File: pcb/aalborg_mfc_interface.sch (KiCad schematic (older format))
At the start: 19 parts, among them J1 DB15FV, J2 DB15FV, P1 PWR_JACK_2.5x5.5, P2 HEADER_01X03, U1 MAX6817

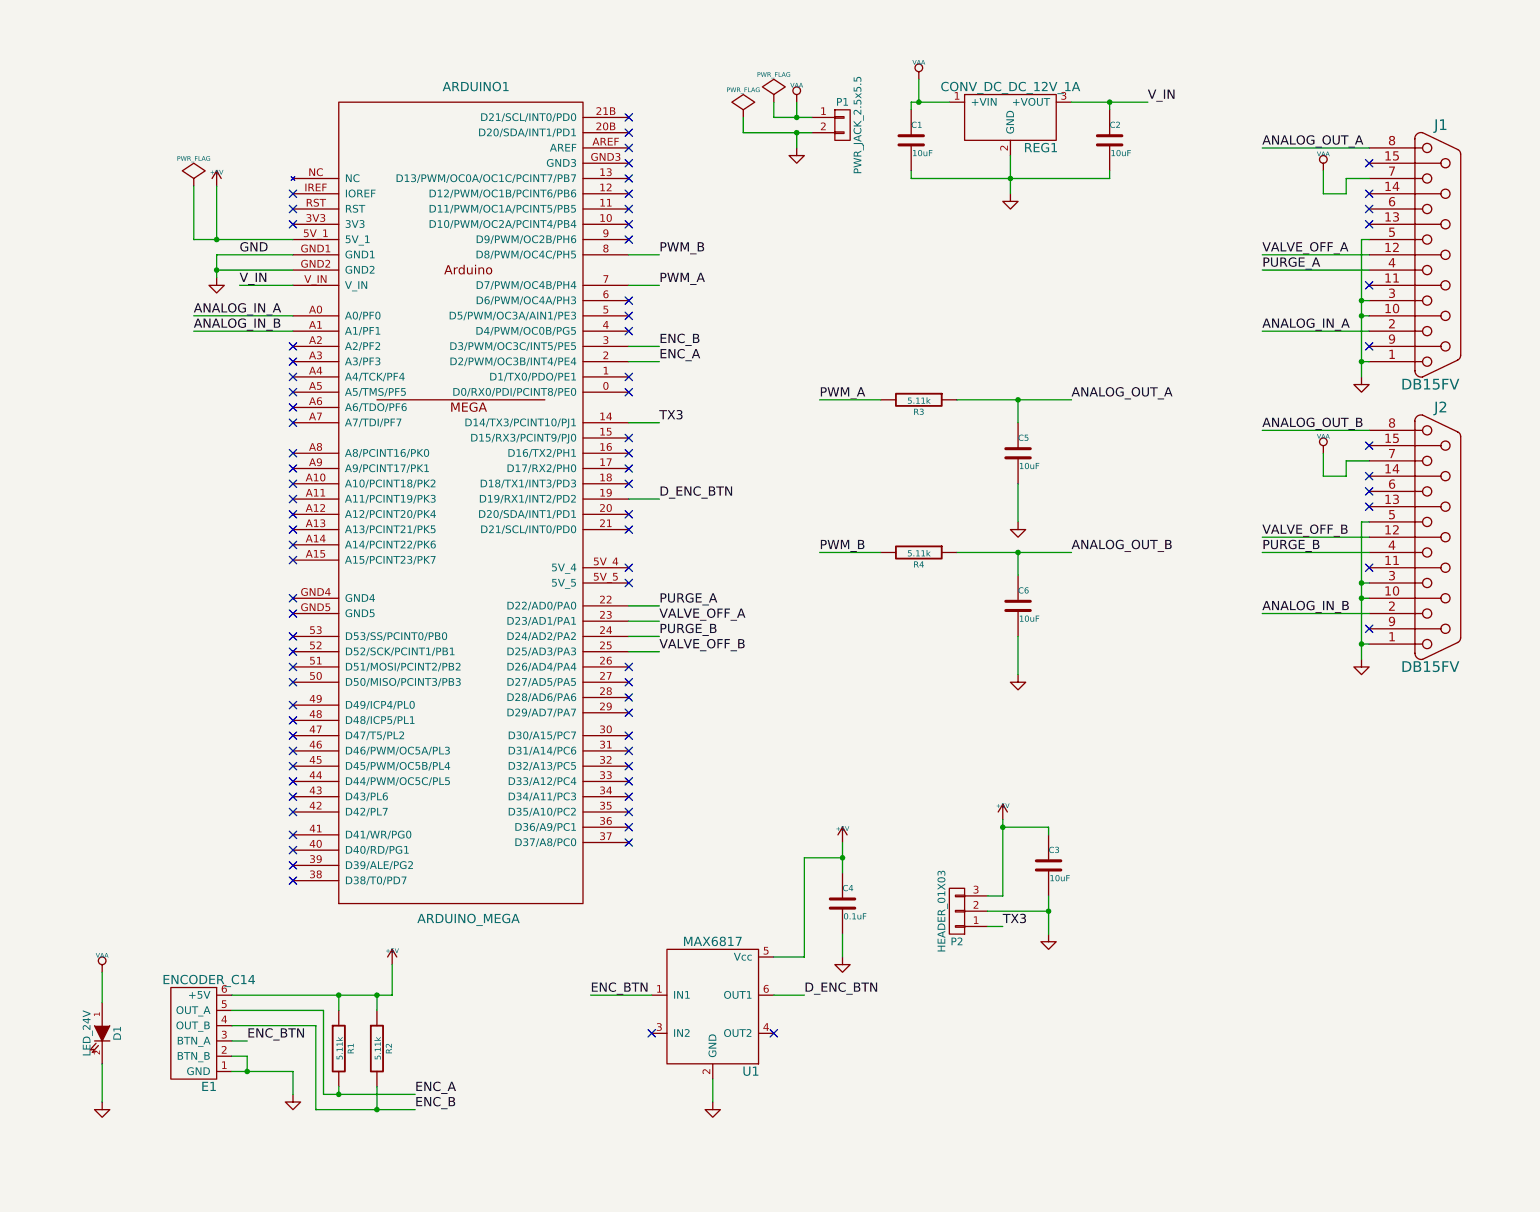
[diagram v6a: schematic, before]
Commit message: Updated design with changes first made to power_switch_controller.
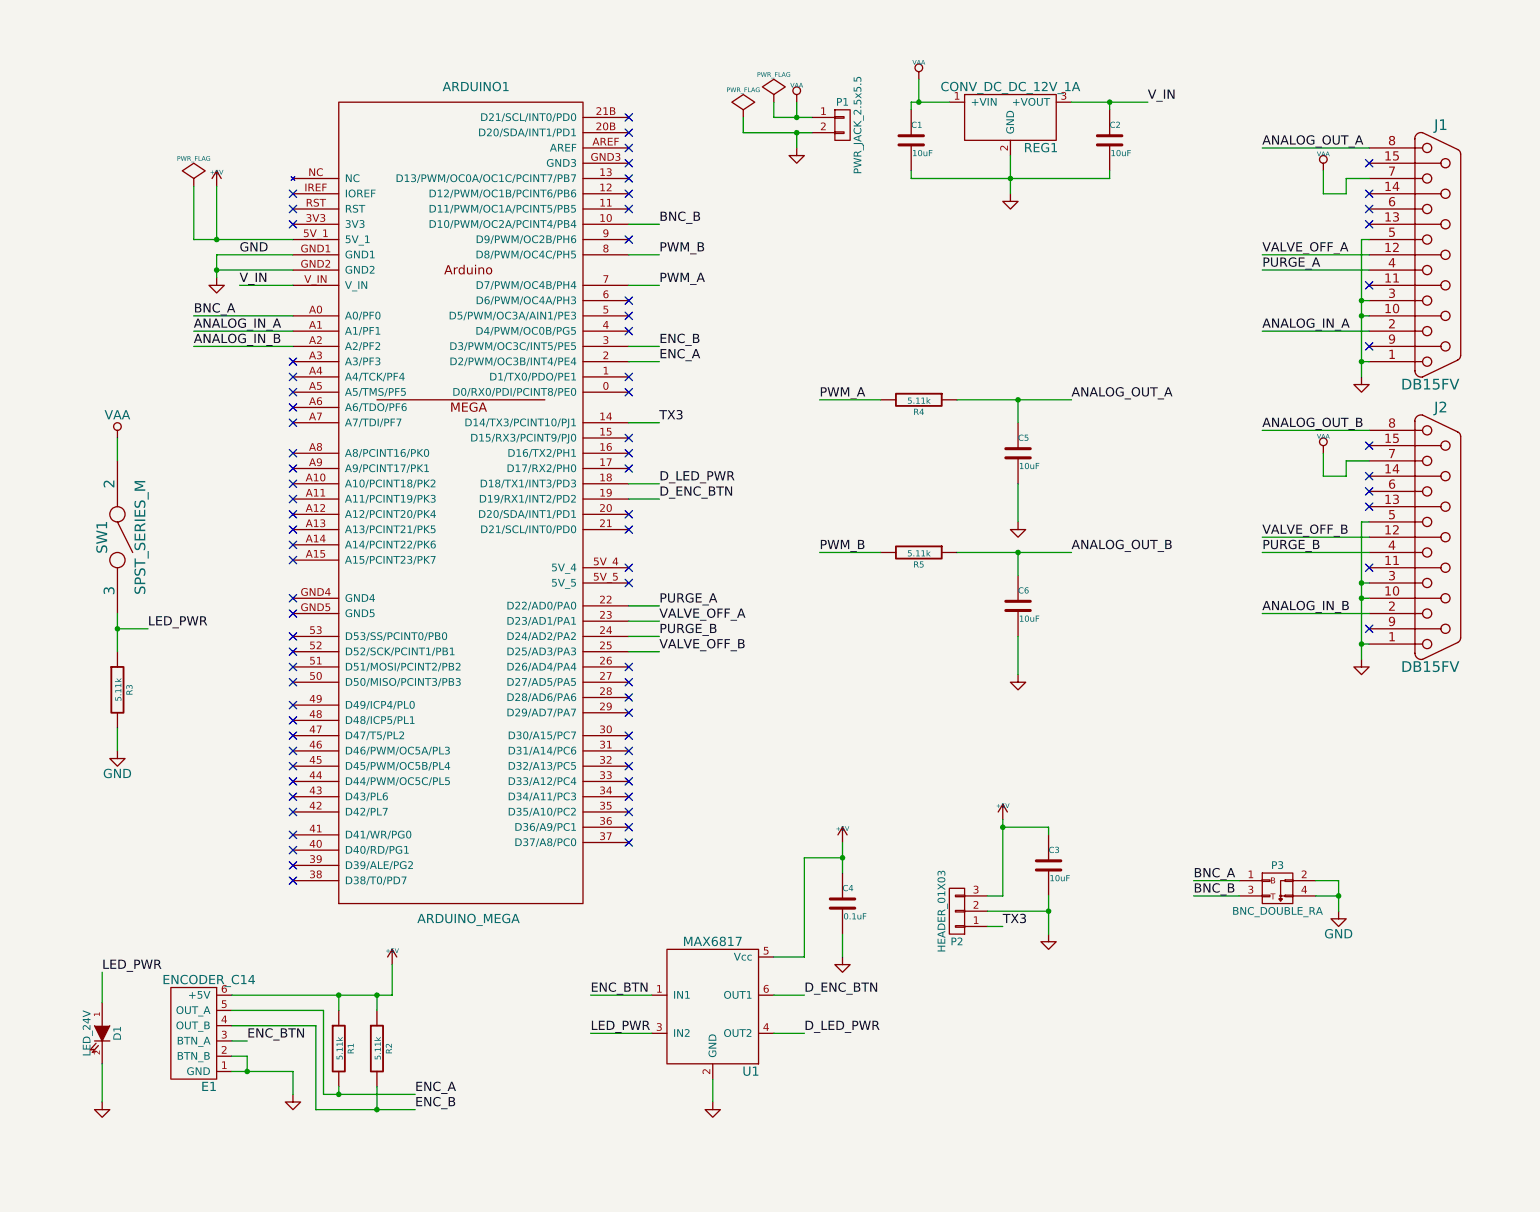
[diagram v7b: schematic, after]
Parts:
- added P3: BNC_DOUBLE_RA, aalborg_mfc_interface:BNC_DOUBLE, symbol BNC_DOUBLE_RA
- added R3: 5.11k, aalborg_mfc_interface:SM1210, symbol 5.11k
- added SW1: SPST_SERIES_M, aalborg_mfc_interface:SPST_SERIES_M, symbol SPST_SERIES_M
- renumbered R3 to R4, R4 to R5
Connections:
- net ANALOG_IN_A: now also ARDUINO1.A1 (A1/PF1); no longer ARDUINO1.A0 (A0/PF0)
- net ANALOG_IN_B: now also ARDUINO1.A2 (A2/PF2); no longer ARDUINO1.A1 (A1/PF1)
- net GND: now also P3.2 (P2), P3.4 (P4), R3.2
- net VAA: now also SW1.2; no longer D1.1 (A)
- net BNC_B: now reaches ARDUINO1.10 (D10/PWM/OC2A/PCINT4/PB4)
- net BNC_B: now also P3.3 (P3)
- net D_LED_PWR: now reaches ARDUINO1.18 (D18/TX1/INT3/PD3)
- net D_LED_PWR: now also U1.4 (OUT2)
- net LED_PWR: now reaches U1.3 (IN2)
- net LED_PWR: now also D1.1 (A), R3.1, SW1.3
- new net BNC_A: ARDUINO1.A0 (A0/PF0), P3.1 (P1)
- no-connect marks 83 -> 78
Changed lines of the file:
@@
 EELAYER 25 0
 EELAYER END
-$Descr A4 11693 8268
+$Descr A 11000 8500
 encoding utf-8
 Sheet 1 1
@@
 	2100 1950 1600 1950
 Connection ~ 1600 1950
-NoConn ~ 2100 2450
 NoConn ~ 2100 2550
 NoConn ~ 2100 2650
@@
 NoConn ~ 4300 1450
 NoConn ~ 4300 1550
-NoConn ~ 4300 1650
 NoConn ~ 4300 1750
 NoConn ~ 4300 2150
@@
 NoConn ~ 4300 3150
 NoConn ~ 4300 3250
-NoConn ~ 4300 3350
 NoConn ~ 4300 3550
 NoConn ~ 4300 3650
@@
 Wire Wire Line
 	4850 7250 4850 7400
-NoConn ~ 4450 6950
-NoConn ~ 5250 6950
 $Comp
 L GND #PWR017
@@
 Text Label 8450 2350 0    60   ~ 0
 ANALOG_IN_A
-$Comp
-L VAA #PWR020
-U 1 1 547DE3D4
-P 850 6550
-F 0 "#PWR020" H 850 6610 30  0001 C CNN
-F 1 "VAA" H 850 6660 30  0000 C CNN
-F 2 "" H 850 6550 60  0000 C CNN
-F 3 "" H 850 6550 60  0000 C CNN
-	1    850  6550
-	1    0    0    -1
-$EndComp
 Wire Wire Line
 	2100 2250 1450 2250
-Text Label 1450 2250 0    60   ~ 0
+Text Label 1450 2350 0    60   ~ 0
 ANALOG_IN_A
-Wire Wire Line
-	2100 2350 1450 2350
-Text Label 1450 2350 0    60   ~ 0
+Text Label 1450 2450 0    60   ~ 0
 ANALOG_IN_B
 Wire Wire Line
@@
 PWM_B
 $Comp
-L GND #PWR021
+L GND #PWR020
 U 1 1 547E11DE
 P 6850 3600
-F 0 "#PWR021" H 6850 3600 30  0001 C CNN
+F 0 "#PWR020" H 6850 3600 30  0001 C CNN
 F 1 "GND" H 6850 3530 30  0001 C CNN
 F 2 "" H 6850 3600 60  0000 C CNN
@@
 PWM_A
 $Comp
-L GND #PWR022
+L GND #PWR021
 U 1 1 547E1CA6
 P 6850 4600
-F 0 "#PWR022" H 6850 4600 30  0001 C CNN
+F 0 "#PWR021" H 6850 4600 30  0001 C CNN
 F 1 "GND" H 6850 4530 30  0001 C CNN
 F 2 "" H 6850 4600 60  0000 C CNN
@@
 PWM_B
 $Comp
-L GND #PWR023
+L GND #PWR022
 U 1 1 547E1DFB
 P 9100 4500
-F 0 "#PWR023" H 9100 4500 30  0001 C CNN
+F 0 "#PWR022" H 9100 4500 30  0001 C CNN
 F 1 "GND" H 9100 4430 30  0001 C CNN
 F 2 "" H 9100 4500 60  0000 C CNN
@@
 ANALOG_OUT_B
 $Comp
-L VAA #PWR024
+L VAA #PWR023
 U 1 1 547E1E15
 P 8850 3150
-F 0 "#PWR024" H 8850 3210 30  0001 C CNN
+F 0 "#PWR023" H 8850 3210 30  0001 C CNN
 F 1 "VAA" H 8850 3260 30  0000 C CNN
 F 2 "" H 8850 3150 60  0000 C CNN
@@
 $EndComp
 $Comp
-L 5.11k R3
+L 5.11k R4
 U 1 1 54894188
 P 6200 2800
-F 0 "R3" V 6280 2800 40  0000 C CNN
+F 0 "R4" V 6280 2800 40  0000 C CNN
 F 1 "5.11k" V 6207 2801 40  0000 C CNN
 F 2 "aalborg_mfc_interface:SM1210" V 6130 2800 30  0001 C CNN
@@
 $EndComp
 $Comp
-L 5.11k R4
+L 5.11k R5
 U 1 1 5489443F
 P 6200 3800
-F 0 "R4" V 6280 3800 40  0000 C CNN
+F 0 "R5" V 6280 3800 40  0000 C CNN
 F 1 "5.11k" V 6207 3801 40  0000 C CNN
 F 2 "aalborg_mfc_interface:SM1210" V 6130 3800 30  0001 C CNN
@@
 	1    6200 3800
 	0    1    1    0
-$EndComp
-$Comp
-L ARDUINO_MEGA ARDUINO1
-U 1 1 5489C516
-P 3250 3500
-F 0 "ARDUINO1" H 3300 6250 60  0000 C CNN
-F 1 "ARDUINO_MEGA" H 3250 800 60  0000 C CNN
-F 2 "aalborg_mfc_interface:ARDUINO_MEGA_SHIELD" H 3200 6150 60  0001 C CNN
-F 3 "" H 3300 6250 60  0000 C CNN
-F 4 "digikey" H 3400 6350 60  0001 C CNN "Vendor"
-F 5 "1050-1018-ND" H 3500 6450 60  0001 C CNN "PartNumber"
-F 6 "BOARD MCU MEGA2560" H 3600 6550 60  0001 C CNN "Description"
-	1    3250 3500
-	1    0    0    -1
 $EndComp
 $Comp
@@
 	1    0    0    -1
 $EndComp
+$Comp
+L ARDUINO_MEGA ARDUINO1
+U 1 1 54AEFE62
+P 3250 3500
+F 0 "ARDUINO1" H 3300 6250 60  0000 C CNN
+F 1 "ARDUINO_MEGA" H 3250 800 60  0000 C CNN
+F 2 "aalborg_mfc_interface:ARDUINO_MEGA_SHIELD" H 3200 6150 60  0001 C CNN
+F 3 "" H 3300 6250 60  0000 C CNN
+F 4 "digikey" H 3400 6350 60  0001 C CNN "Vendor"
+F 5 "1050-1018-ND" H 3500 6450 60  0001 C CNN "PartNumber"
+F 6 "BOARD MCU MEGA2560" H 3600 6550 60  0001 C CNN "Description"
+	1    3250 3500
+	1    0    0    -1
+$EndComp
+Wire Wire Line
+	2100 2450 1450 2450
+Wire Wire Line
+	2100 2350 1450 2350
+Text Label 1450 2250 0    60   ~ 0
+BNC_A
+Wire Wire Line
+	4300 1650 4500 1650
+Text Label 4500 1650 0    60   ~ 0
+BNC_B
+Wire Wire Line
+	4300 3350 4500 3350
+Text Label 4500 3350 0    60   ~ 0
+D_LED_PWR
+Text Label 850  6550 0    60   ~ 0
+LED_PWR
+Wire Wire Line
+	4450 6950 4050 6950
+Text Label 4050 6950 0    60   ~ 0
+LED_PWR
+Wire Wire Line
+	5250 6950 5450 6950
+Text Label 5450 6950 0    60   ~ 0
+D_LED_PWR
+$Comp
+L BNC_DOUBLE_RA P3
+U 1 1 54AF19CE
+P 8550 6000
+F 0 "P3" H 8550 6150 50  0000 C CNN
+F 1 "BNC_DOUBLE_RA" H 8550 5850 50  0000 C CNN
+F 2 "aalborg_mfc_interface:BNC_DOUBLE" H 8550 4800 60  0001 C CNN
+F 3 "" H 8550 4800 60  0000 C CNN
+F 4 "digikey" H 8650 6250 60  0001 C CNN "Vendor"
+F 5 "ACX1655-ND" H 8750 6350 60  0001 C CNN "PartNumber"
+F 6 "CONN BNC JACK R/A 75 OHM PCB" H 8850 6450 60  0001 C CNN "Description"
+	1    8550 6000
+	1    0    0    -1
+$EndComp
+$Comp
+L GND #PWR024
+U 1 1 54AF1B06
+P 8950 6150
+F 0 "#PWR024" H 8950 5900 60  0001 C CNN
+F 1 "GND" H 8950 6000 60  0000 C CNN
+F 2 "" H 8950 6150 60  0000 C CNN
+F 3 "" H 8950 6150 60  0000 C CNN
+	1    8950 6150
+	1    0    0    -1
+$EndComp
+Wire Wire Line
+	8800 5950 8950 5950
+Wire Wire Line
+	8950 5950 8950 6150
+Wire Wire Line
+	8800 6050 8950 6050
+Connection ~ 8950 6050
+Wire Wire Line
+	8300 5950 8000 5950
+Wire Wire Line
+	8300 6050 8000 6050
+Text Label 8000 5950 0    60   ~ 0
+BNC_A
+Text Label 8000 6050 0    60   ~ 0
+BNC_B
+$Comp
+L SPST_SERIES_M SW1
+U 1 1 54AF2791
+P 950 3700
+F 0 "SW1" H 950 3600 70  0000 C CNN
+F 1 "SPST_SERIES_M" H 950 3850 70  0000 C CNN
+F 2 "aalborg_mfc_interface:SPST_SERIES_M" H 850 3500 60  0001 C CNN
+F 3 "" H 950 3700 60  0000 C CNN
+F 4 "digikey" H 1050 3900 60  0001 C CNN "Vendor"
+F 5 "360-3243-ND" H 1150 4000 60  0001 C CNN "PartNumber"
+F 6 "SWITCH TOGGLE SPST 6A 125V" H 1250 4100 60  0001 C CNN "Description"
+	1    950  3700
+	0    1    1    0
+$EndComp
+$Comp
+L VAA #PWR025
+U 1 1 54AF28AD
+P 950 3050
+F 0 "#PWR025" H 950 2900 60  0001 C CNN
+F 1 "VAA" H 950 3200 60  0000 C CNN
+F 2 "" H 950 3050 60  0000 C CNN
+F 3 "" H 950 3050 60  0000 C CNN
+	1    950  3050
+	1    0    0    -1
+$EndComp
+Wire Wire Line
+	950  3050 950  3200
+$Comp
+L 5.11k R3
+U 1 1 54AF2C25
+P 950 4700
+F 0 "R3" V 1030 4700 40  0000 C CNN
+F 1 "5.11k" V 957 4701 40  0000 C CNN
+F 2 "aalborg_mfc_interface:SM1210" V 880 4700 30  0001 C CNN
+F 3 "" H 950 4700 30  0000 C CNN
+F 4 "digikey" V 1130 4800 60  0001 C CNN "Vendor"
+F 5 "P5.11KAACT-ND" V 1230 4900 60  0001 C CNN "PartNumber"
+F 6 "RES SMD 5.11K OHM 1% 1/2W 1210" V 1330 5000 60  0001 C CNN "Description"
+	1    950  4700
+	1    0    0    -1
+$EndComp
+$Comp
+L GND #PWR026
+U 1 1 54AF2C77
+P 950 5100
+F 0 "#PWR026" H 950 4850 60  0001 C CNN
+F 1 "GND" H 950 4950 60  0000 C CNN
+F 2 "" H 950 5100 60  0000 C CNN
+F 3 "" H 950 5100 60  0000 C CNN
+	1    950  5100
+	1    0    0    -1
+$EndComp
+Wire Wire Line
+	950  4200 950  4450
+Wire Wire Line
+	950  4950 950  5100
+Wire Wire Line
+	950  4300 1150 4300
+Connection ~ 950  4300
+Text Label 1150 4300 0    60   ~ 0
+LED_PWR
 $EndSCHEMATC

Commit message: Incremental changes towards version 1.1.
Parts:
- removed P3: BNC_DOUBLE_RA, aalborg_mfc_interface:BNC_DOUBLE, symbol BNC_DOUBLE_RA
- added C7: 10uF, aalborg_mfc_interface:SM1210, symbol 10uF
- added J3: DB15FV, aalborg_mfc_interface:DB15FD, symbol DB15FV
- added P3, P4, P5: HEADER_01X03, aalborg_mfc_interface:Header_Shrouded_3_Pin, symbol HEADER_01X03
- added R6: 5.11k, aalborg_mfc_interface:SM1210, symbol 5.11k
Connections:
- net +5V: now also P3.2 (P2), P4.2 (P2), P5.2 (P2)
- net GND: now also C7.2, J3.1, J3.10 (P10), J3.3, J3.5, P3.3 (P3), P4.3 (P3), P5.3 (P3)
- net VAA: now also J3.7
- net PURGE_2: now reaches ARDUINO1.26 (D26/AD4/PA4)
- net PURGE_2: now also J3.4
- net VALVE_OFF_2: now reaches ARDUINO1.27 (D27/AD5/PA5)
- net VALVE_OFF_2: now also J3.12 (P12)
- net PWM_2: now reaches ARDUINO1.9 (D9/PWM/OC2B/PH6)
- net PWM_2: now also R6.2
- net ANALOG_IN_0: now reaches ARDUINO1.A3 (A3/PF3)
- net ANALOG_IN_0: now also J1.2
- net ANALOG_IN_1: now reaches ARDUINO1.A4 (A4/TCK/PF4)
- net ANALOG_IN_1: now also J2.2
- net ANALOG_IN_2: now reaches ARDUINO1.A5 (A5/TMS/PF5)
- net ANALOG_IN_2: now also J3.2
- net ANALOG_IN_A renamed A1
- net A1: now also P4.1 (P1); no longer J1.2
- net ANALOG_IN_B renamed A2
- net A2: now also P5.1 (P1); no longer J2.2
- net ANALOG_OUT_A renamed ANALOG_OUT_0
- net ANALOG_OUT_B renamed ANALOG_OUT_1
- net BNC_A renamed A0
- net A0: now also P3.1 (P1)
- net BNC_B: no longer names the net of ARDUINO1.10 (D10/PWM/OC2A/PCINT4/PB4)
- net PURGE_A renamed PURGE_0
- net PURGE_B renamed PURGE_1
- net PWM_A renamed PWM_0
- net PWM_B renamed PWM_1
- net VALVE_OFF_A renamed VALVE_OFF_0
- net VALVE_OFF_B renamed VALVE_OFF_1
- new net ANALOG_OUT_2: C7.1, J3.8, R6.1
- no-connect marks 78 -> 79
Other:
- moved on the sheet: C3, C5, C6, J1, J2, P2, R4, R5
